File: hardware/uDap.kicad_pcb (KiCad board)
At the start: 2 copper layers, 11 x 11.7 mm, 6 parts, among them J1 USB_C_Receptacle_USB2.0_16P, J2 Conn_02x04_Odd_Even, U1 CH32X035F8U6, U2 RT9013

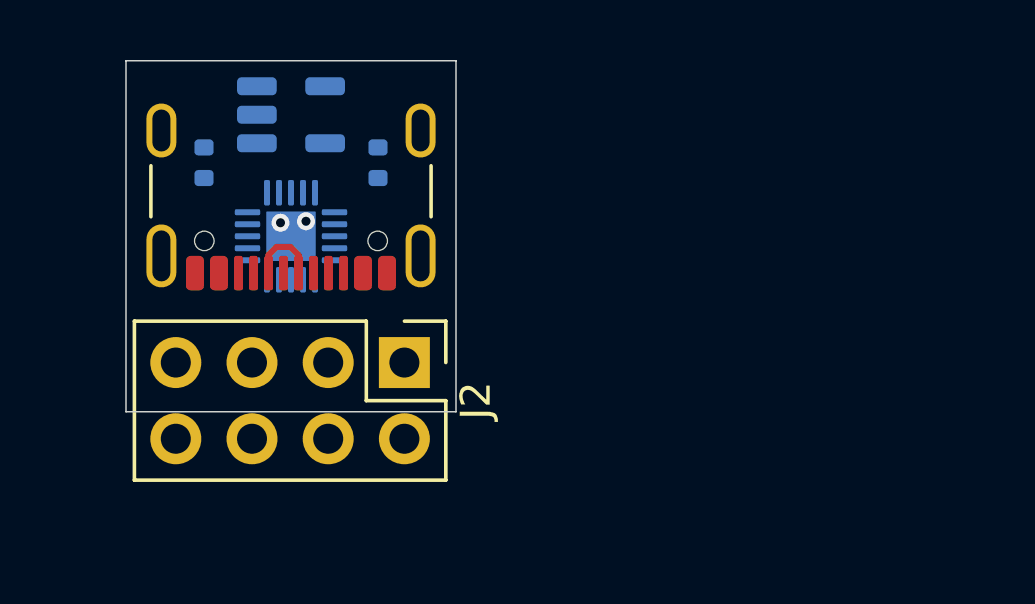
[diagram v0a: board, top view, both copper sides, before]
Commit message: 完善了 udap-ch32x035 整体的功能
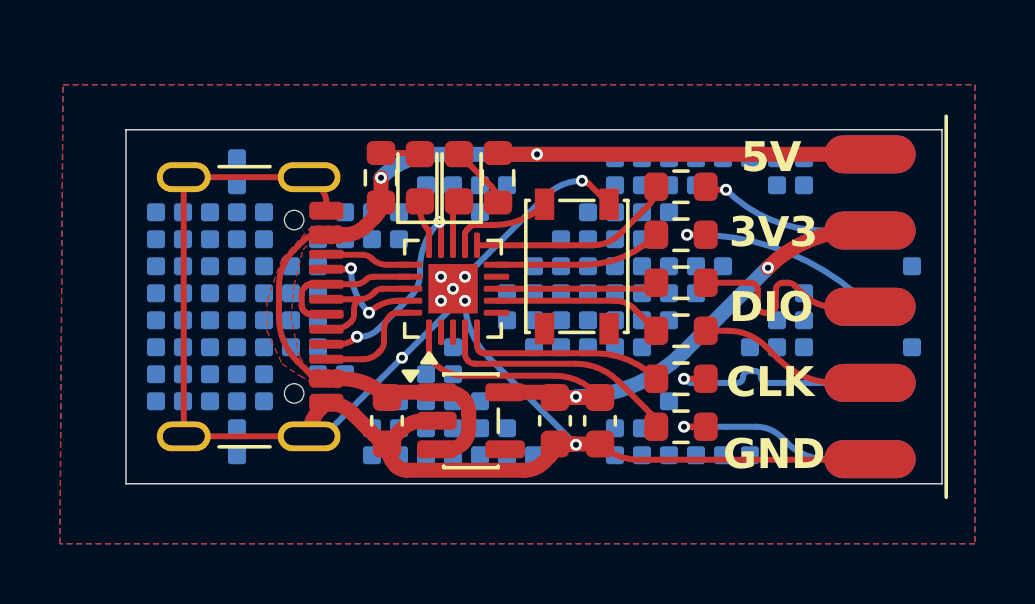
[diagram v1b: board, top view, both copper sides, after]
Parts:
- removed J2: Conn_02x04_Odd_Even, Connector_PinHeader_2.54mm:PinHeader_2x04_P2.54mm_Vertical
- added C1: 1uF, Capacitor_SMD:C_0603_1608Metric, F.Cu at (111.7, 91.3)
- added C2: 1uF, Capacitor_SMD:C_0603_1608Metric, F.Cu at (117.3, 91.3)
- added C3: 0.1uF, Capacitor_SMD:C_0603_1608Metric, F.Cu at (118.8, 91.3)
- added D1: LED, LED_SMD:LED_0603_1608Metric, F.Cu at (114.1, 83.2)
- added D2: LED, LED_SMD:LED_0603_1608Metric, F.Cu at (112.8, 83.2)
- added J3: Conn_02x05_Odd_Even, my_connector:双面贴片排针2x5, F.Cu at (127.8, 87.5)
- added R3: 47R, Resistor_SMD:R_0603_1608Metric, F.Cu at (121.5, 86.7)
- added R4: 47R, Resistor_SMD:R_0603_1608Metric, F.Cu at (121.5, 88.3)
- added R5: 47R, Resistor_SMD:R_0603_1608Metric, F.Cu at (121.5, 89.9)
- added R6: 47R, Resistor_SMD:R_0603_1608Metric, F.Cu at (121.5, 91.5)
- added R7: 4.7K, Resistor_SMD:R_0603_1608Metric, F.Cu at (115.4, 83.2)
- added R9: 4.7K, Resistor_SMD:R_0603_1608Metric, F.Cu at (111.5, 83.2)
- added SW3: SW_MEC_5E, my_footprint:KEY-SMD_4P-L4.2-W3.4-P2.15-LS4.5-TL_1, F.Cu at (118.1, 86.1)
- R1, R2: value 5.1k -> 47R; footprint Resistor_SMD:R_0402_1005Metric -> Resistor_SMD:R_0603_1608Metric; moved to F.Cu
- U1, U2: moved to F.Cu
- moved R1 15.9 mm to (121.5, 83.5), turned to 0 degrees
- moved U2 11.8 mm to (114.5, 91.3)
- moved R2 10.4 mm to (121.5, 85.1), turned to 0 degrees
- moved U1 5.68 mm to (113.9, 86.9), turned to 90 degrees
- moved J1 5.41 mm to (106.0, 87.5), turned to -90 degrees
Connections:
- J1 pad A5: Net-(J1-CC1) -> /CC1
- J1 pad A8: unconnected-(J1-SBU1-PadA8) -> /RVDIO
- J1 pad B5: Net-(J1-CC2) -> /CC2
- J1 pad B8: unconnected-(J1-SBU2-PadB8) -> /RVDCK
- R1 pad 1: Net-(J1-CC2) -> /RX
- R1 pad 2: GND -> /RX_
- R2 pad 1: Net-(J1-CC1) -> /TX
- R2 pad 2: GND -> /TX_
- U1 pad 1: unconnected-(U1-VDD-Pad1) -> +3V3
- U1 pad 10: unconnected-(U1-PB0-Pad10) -> /TX
- U1 pad 11: unconnected-(U1-PB1-Pad11) -> /RX
- U1 pad 12: unconnected-(U1-PB3-Pad12) -> Net-(U1-PB3)
- U1 pad 13: unconnected-(U1-PB11-Pad13) -> /LED_DAP
- U1 pad 14: unconnected-(U1-PC18-Pad14) -> /RVDIO
- U1 pad 15: unconnected-(U1-PB12-Pad15) -> /LED_UART
- U1 pad 16: unconnected-(U1-PC19-Pad16) -> /RVDCK
- U1 pad 19: Net-(J1-CC1) -> /CC1
- U1 pad 20: Net-(J1-CC2) -> /CC2
- U1 pad 4: unconnected-(U1-PA2-Pad4) -> /TX2
- U1 pad 5: unconnected-(U1-PA3-Pad5) -> /RX2
- U1 pad 7: unconnected-(U1-PA5-Pad7) -> /CLK
- U1 pad 8: unconnected-(U1-PA6-Pad8) -> /DIO
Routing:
- net GND: track 0.00 -> 61.2 mm, vias 2 -> 8
- net +5V: track 0.00 -> 35.1 mm, vias 0 -> 2
- net +3V3: track 0.00 -> 21.8 mm, vias 0 -> 2
- net /TX2: track 0.00 -> 8.17 mm
- net /RX2_: track 0.00 -> 7.39 mm, vias 0 -> 1
- net /TX_: track 0.00 -> 7.33 mm, vias 0 -> 1
- net /DIO_: track 0.00 -> 7.27 mm
- net /TX2_: track 0.00 -> 7.23 mm, vias 0 -> 1
- net /RVDIO: track 0.00 -> 7.14 mm, vias 0 -> 2
- net /RX: track 0.00 -> 6.89 mm
- net /RX2: track 0.00 -> 6.78 mm
- net /CLK_: track 0.00 -> 5.98 mm
- net /RX_: track 0.00 -> 5.84 mm, vias 0 -> 1
- net /CLK: track 0.00 -> 5.70 mm
- net /DIO: track 0.00 -> 5.64 mm
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- added copper zone on F.Cu, net +5V
- added copper zone on B.Cu, net GND
- added copper zone on F.Cu, net GND
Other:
- board size 11 x 11.7 mm -> 27.2 x 11.8 mm
- board text added: "3V3"
- board text added: "5V"
- board text added: "CLK"
- board text added: "DIO"
- board text added: "DTR"
- board text added: "GND"
- board text added: "PC"
- board text added: "RST"
- board text added: "RTS"
- board text added: "RVSWD"
- board text added: "RX"
- board text added: "RX1"
- board text added: "RX2"
- board text added: "SWD"
- board text added: "TX"
- board text added: "TX1"
- board text added: "TX2"
- board text added: "UART0/1"
- board text added: "uDap"
